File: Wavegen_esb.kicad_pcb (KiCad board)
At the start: 4 copper layers, 118 parts, among them IC1 PA107DP, IC2 PA107DP, J1 USB_C_Receptacle_USB2.0_16P, J2 Conn_01x01_Pin, J3 2601-1102, SW1 SW_SPST, SW2 SW_SPST, T1 WE-PPTI_1006, U14 MT3608, U2 ADUM4160, U4 AD8014ARZ, U5 LMH6881SQ/NOPB, U6 AD9834, U7 USBLC6-2SC6, U8 DS8572-33S5, U9 STM32F072CBTx, Y1 ASE-xxxMHz

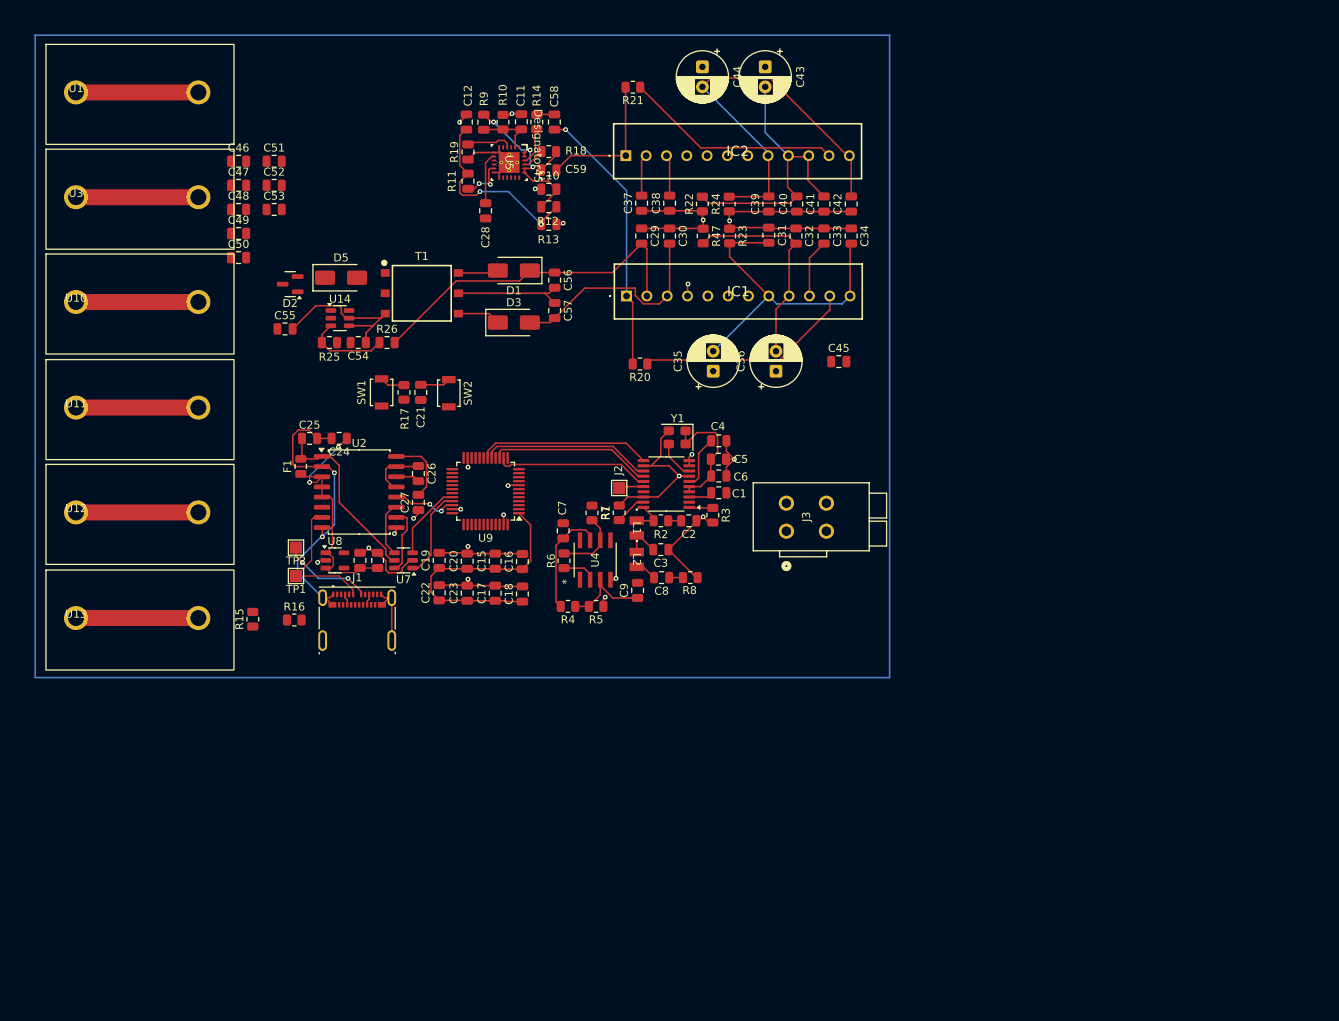
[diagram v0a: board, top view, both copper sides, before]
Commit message: sim the new lpf
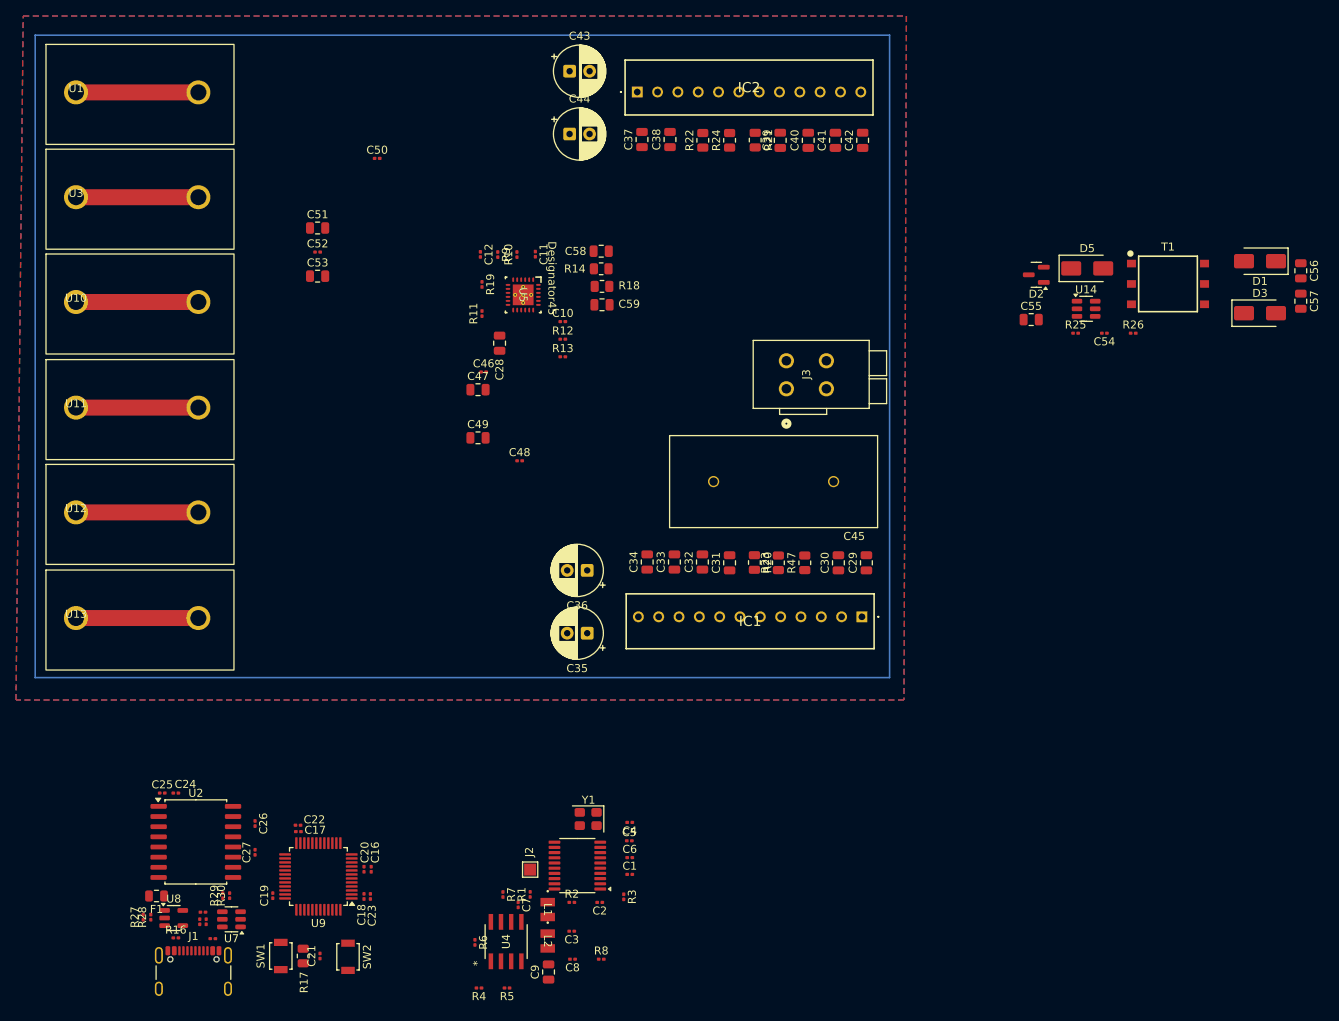
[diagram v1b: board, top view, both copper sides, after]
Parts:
- removed TP1, TP2: TestPoint, TestPoint:TestPoint_Pad_1.5x1.5mm
- added R27: 24, Resistor_SMD:R_0201_0603Metric, F.Cu at (84.7, 137.0)
- added R28: 24, Resistor_SMD:R_0201_0603Metric, F.Cu at (85.7, 137.0)
- added R29: 24, Resistor_SMD:R_0201_0603Metric, F.Cu at (94.7, 134.4)
- added R30: 24, Resistor_SMD:R_0201_0603Metric, F.Cu at (95.5, 134.4)
- C1, C13, C14, C15, C16, C17, C18, C19, C2, C20, C21, C22, C23, C24, C25, C26, C27, C3, C4, C46, C48, C5, C50, C52, C54, C6, C7, C8: footprint Capacitor_SMD:C_0805_2012Metric -> Capacitor_SMD:C_0201_0603Metric
- C10: value 0.1pf -> 0.1uf; footprint Capacitor_SMD:C_0805_2012Metric -> Capacitor_SMD:C_0201_0603Metric
- C11, C12: value 0.1pf -> 10uf; footprint Capacitor_SMD:C_0805_2012Metric -> Capacitor_SMD:C_0201_0603Metric
- C45: footprint Capacitor_SMD:C_0805_2012Metric -> 1_cap:CAPRR1500W80L2600T1150H2600
- J1: footprint Connector_USB:USB_C_Receptacle_Molex_105450-0101 -> Connector_USB:USB_C_Receptacle_GCT_USB4105-xx-A_16P_TopMnt_Horizontal
- R1, R10, R15, R16, R2, R3, R4, R5, R6, R7, R8: footprint Resistor_SMD:R_0805_2012Metric -> Resistor_SMD:R_0201_0603Metric
- R11, R12, R13, R19, R25, R26, R9: footprint Capacitor_SMD:C_0805_2012Metric -> Resistor_SMD:R_0201_0603Metric
- R14, R18: value 1k -> 665
- moved C56 93.3 mm to (229.4, 56.2)
- moved C57 93.3 mm to (229.4, 60.0)
- moved D1 93.3 mm to (224.3, 55.0)
- moved D2 93.3 mm to (196.3, 56.8)
- moved D3 93.3 mm to (224.3, 61.5)
- moved T1 93.3 mm to (212.8, 57.9)
- moved C54 93.3 mm to (204.8, 64.0)
- moved R25 93.3 mm to (201.2, 64.0)
- moved U14 93.3 mm to (202.6, 61.0)
- moved C55 93.3 mm to (195.7, 62.4)
- moved D5 93.3 mm to (202.7, 56.0)
- moved R26 93.3 mm to (208.4, 64.0)
- moved C21 71.6 mm to (106.8, 141.9)
- moved R17 71.6 mm to (104.7, 141.9)
- moved SW1 71.6 mm to (101.9, 141.9)
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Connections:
- C12 pad 1: GND -> Net-(C12-Pad1)
- C12 pad 2: Net-(C12-Pad2) -> GND
- C2 pad 2: Net-(C2-Pad2) -> Net-(U6-IOUTB)
- C24 pad 1: +5V -> Net-(U2-PDEN)
- C25 pad 1: VBUS -> Net-(U2-VBUS1)
- C26 pad 2: Net-(U2-VDD2) -> Net-(U2-SPD)
- C27 pad 2: Net-(U2-VBUS2) -> +5V
- C8 pad 1: Net-(C8-Pad1) -> GND
- F1 pad 1: +5V -> Net-(U2-VBUS1)
- J1 pad A6: D+ -> Net-(J1-D+-PadA6)
- J1 pad A7: D- -> Net-(J1-D--PadA7)
- J1 pad B6: D+ -> Net-(J1-D+-PadA6)
- J1 pad B7: D- -> Net-(J1-D--PadA7)
- R11 pad 2: Net-(C12-Pad2) -> Net-(C12-Pad1)
- R12 pad 2: Net-(C12-Pad2) -> Net-(C12-Pad1)
- R13 pad 1: Net-(C12-Pad2) -> Net-(C12-Pad1)
- R2 pad 2: Net-(C2-Pad2) -> GND
- R8 pad 1: Net-(C8-Pad1) -> Net-(C8-Pad2)
- U2 pad 1: VBUS -> Net-(U2-VBUS1)
- U2 pad 10: D+iso -> Net-(U2-DD+)
- U2 pad 11: D-iso -> Net-(U2-DD-)
- U2 pad 13: GND -> Net-(U2-SPD)
- U2 pad 14: Net-(U2-VDD2) -> Net-(U2-SPD)
- U2 pad 16: Net-(U2-VBUS2) -> +5V
- U2 pad 3: +5V -> Net-(U2-PDEN)
- U2 pad 4: +5V -> Net-(U2-PDEN)
- U2 pad 5: +5V -> Net-(U2-PDEN)
- U5 pad 5: unconnected-(U5B-SPI-Pad5) -> +5V
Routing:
- net GND: track 200.6 -> 30.6 mm, vias 23 -> 0
- net /+55v: track 106.8 -> 15.3 mm
- net +5V: track 105.0 -> 15.3 mm, vias 5 -> 0
- net /-55v: track 85.5 -> 15.3 mm
- net +3.3V: track 49.6 -> 0.00 mm
- net +15V: track 48.1 -> 0.00 mm
- net GND_USB: track 46.4 -> 0.00 mm, vias 2 -> 0
- net /PA107/PA_IN: track 34.2 -> 0.00 mm, vias 1 -> 0
- net -15V: track 32.4 -> 0.00 mm
- net /PA107/PA107OUT: track 27.3 -> 0.00 mm
- net /PA108/PA107OUT: track 27.2 -> 0.00 mm
- net VBUS: track 25.8 -> 0.00 mm
- net Net-(C12-Pad2): track 24.6 -> 0.00 mm, vias 2 -> 0
- net /STM32/PB0: track 21.6 -> 0.00 mm
- net /STM32/PA7: track 21.3 -> 0.00 mm
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- added copper zone on B.Cu, net GND
- added copper zone on F.Cu, net GND
- added copper zone on In1.Cu, net GND
- added copper zone on In2.Cu, net GND

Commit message: routing draft 3
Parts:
- removed C46: 100nf, Capacitor_SMD:C_0201_0603Metric
- removed C47: 10uf, Capacitor_SMD:C_0805_2012Metric
- removed U3: ~, 1_Sockets:Untitled
- added C60: 0.1uF, Capacitor_SMD:C_0201_0603Metric, F.Cu at (147.5, 67.6)
- added C61: 10uf, Capacitor_THT:C_Radial_D5.0mm_H5.0mm_P2.00mm, F.Cu at (142.4, 61.3)
- added C62: 100pF, Capacitor_SMD:C_0805_2012Metric, F.Cu at (136.7, 72.1)
- added C63: 100pF, Capacitor_SMD:C_0805_2012Metric, F.Cu at (147.6, 69.9)
- added R31: 1k, Resistor_SMD:R_0805_2012Metric, F.Cu at (135.9, 68.9)
- added R32: 1k, Resistor_SMD:R_0805_2012Metric, F.Cu at (146.9, 62.3)
- added R33: 5k, Resistor_SMD:R_0805_2012Metric, F.Cu at (147.6, 65.4)
- C2: value 820pf -> 220pf
- C28: value 4.7uf -> 1uf; footprint Capacitor_SMD:C_0805_2012Metric -> Capacitor_SMD:C_0201_0603Metric
- C3: value 1.43nf -> 620pF
- C7: value 0.1uf -> 0.1uF
- C8: value 820pf -> 300pf
- C9: value 2uf -> 10uf; footprint Capacitor_SMD:C_0805_2012Metric -> Capacitor_THT:C_Radial_D5.0mm_H5.0mm_P2.00mm
- L1: value 39uH -> 22uH
- L2: value 39uH -> 27uH
- R4, R5: value 2.6k -> 100k; footprint Resistor_SMD:R_0201_0603Metric -> Resistor_SMD:R_0805_2012Metric
- R6: value 510 -> 5k; footprint Resistor_SMD:R_0201_0603Metric -> Resistor_SMD:R_0805_2012Metric
- R7: value 51 -> 50
- U4: value AD8014ARZ -> OPA2192IDR; footprint 1_High-speed analog interface:R_8_ADI -> 1_preamp:DGK0008A_N_TEX
- moved C56 125.2 mm to (105.0, 42.2), turned to 0 degrees
- moved C57 122.0 mm to (108.8, 42.2), turned to 0 degrees
- moved D1 120.8 mm to (103.8, 47.3), turned to -90 degrees
- moved D3 114.9 mm to (110.2, 47.3), turned to 90 degrees
- moved T1 106.2 mm to (106.6, 58.8), turned to 90 degrees
- moved D5 98.9 mm to (104.7, 68.9), turned to 90 degrees
- moved R26 95.7 mm to (112.8, 63.1), turned to 90 degrees
- moved U14 93.2 mm to (109.7, 69.0), turned to 90 degrees
- moved D2 92.8 mm to (105.5, 75.3), turned to -90 degrees
- moved C54 92.1 mm to (112.8, 66.8), turned to -90 degrees
- moved R25 88.7 mm to (112.8, 70.3), turned to 90 degrees
- moved C55 85.7 mm to (111.0, 75.9), turned to 90 degrees
- moved R6 75.9 mm to (135.9, 64.9), turned to 90 degrees
- moved U4 74.8 mm to (142.1, 66.3), turned to 0 degrees
- moved R8 73.4 mm to (128.8, 70.0)
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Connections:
- C58 pad 1: /PA107/PA_IN -> Net-(C58-Pad1)
- C58 pad 2: Net-(C58-Pad2) -> Net-(U5A-OUTP)
- C59 pad 1: /PA108/PA_IN -> Net-(C59-Pad1)
- C59 pad 2: Net-(C59-Pad2) -> Net-(U5A-OUTM)
- C7 pad 1: GND -> /VGA/-V
- C7 pad 2: +5V -> GND
- C9 pad 1: Net-(U4-+IN) -> /VGA/-V
- C9 pad 2: Net-(C8-Pad2) -> GND
- R14 pad 1: Net-(U5A-OUTP) -> Net-(C58-Pad1)
- R14 pad 2: Net-(C58-Pad2) -> Net-(C63-Pad1)
- R18 pad 1: Net-(U5A-OUTM) -> Net-(C59-Pad1)
- R18 pad 2: Net-(C59-Pad2) -> Net-(C62-Pad1)
- R4 pad 1: Net-(U4-+IN) -> Net-(C59-Pad1)
- R4 pad 2: +5V -> GND
- R5 pad 1: GND -> Net-(C58-Pad1)
- R5 pad 2: Net-(U4-+IN) -> GND
- R6 pad 1: Net-(U4-OUT) -> /VGA/-INa
- R6 pad 2: Net-(U4--IN) -> /PA107/PA_IN
- R7 pad 2: Net-(U4-OUT) -> Net-(C8-Pad2)
- U4 pad 1: unconnected-(U4-NC-Pad1) -> /PA107/PA_IN
- U4 pad 2: Net-(U4--IN) -> /VGA/-INa
- U4 pad 3: Net-(U4-+IN) -> Net-(C62-Pad1)
- U4 pad 4: GND -> /VGA/-V
- U4 pad 5: unconnected-(U4-NC-Pad5) -> Net-(C63-Pad1)
- U4 pad 6: Net-(U4-OUT) -> /VGA/-INb
- U4 pad 7: +5V -> /PA108/PA_IN
- U4 pad 8: unconnected-(U4-NC-Pad8) -> /VGA/+V
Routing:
- net -5V: track 15.3 -> 0.00 mm
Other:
- board outline added: 97.8 x 68 mm
